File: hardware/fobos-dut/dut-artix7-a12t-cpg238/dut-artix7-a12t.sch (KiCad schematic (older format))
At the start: 4 parts

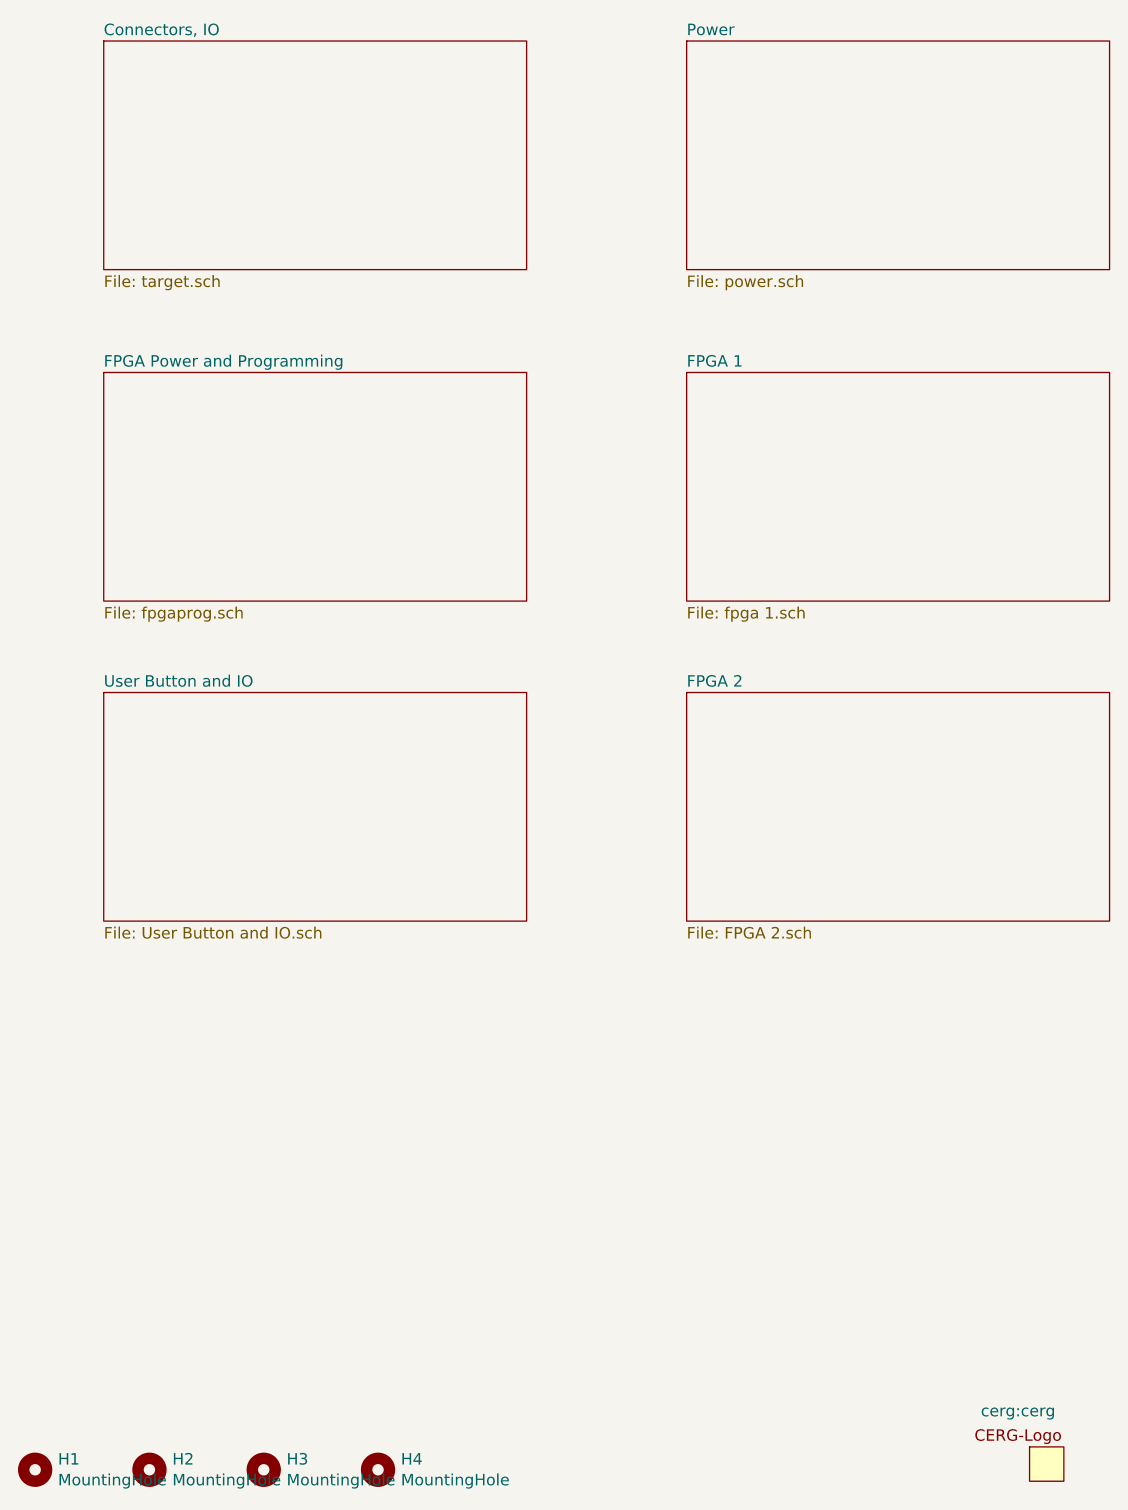
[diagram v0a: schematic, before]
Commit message: Started to rewire the CPG238 into the schematic Split FPGA Power and Programming into two sheets since new FPGA symbol explicitly displays each power pin and is much larger
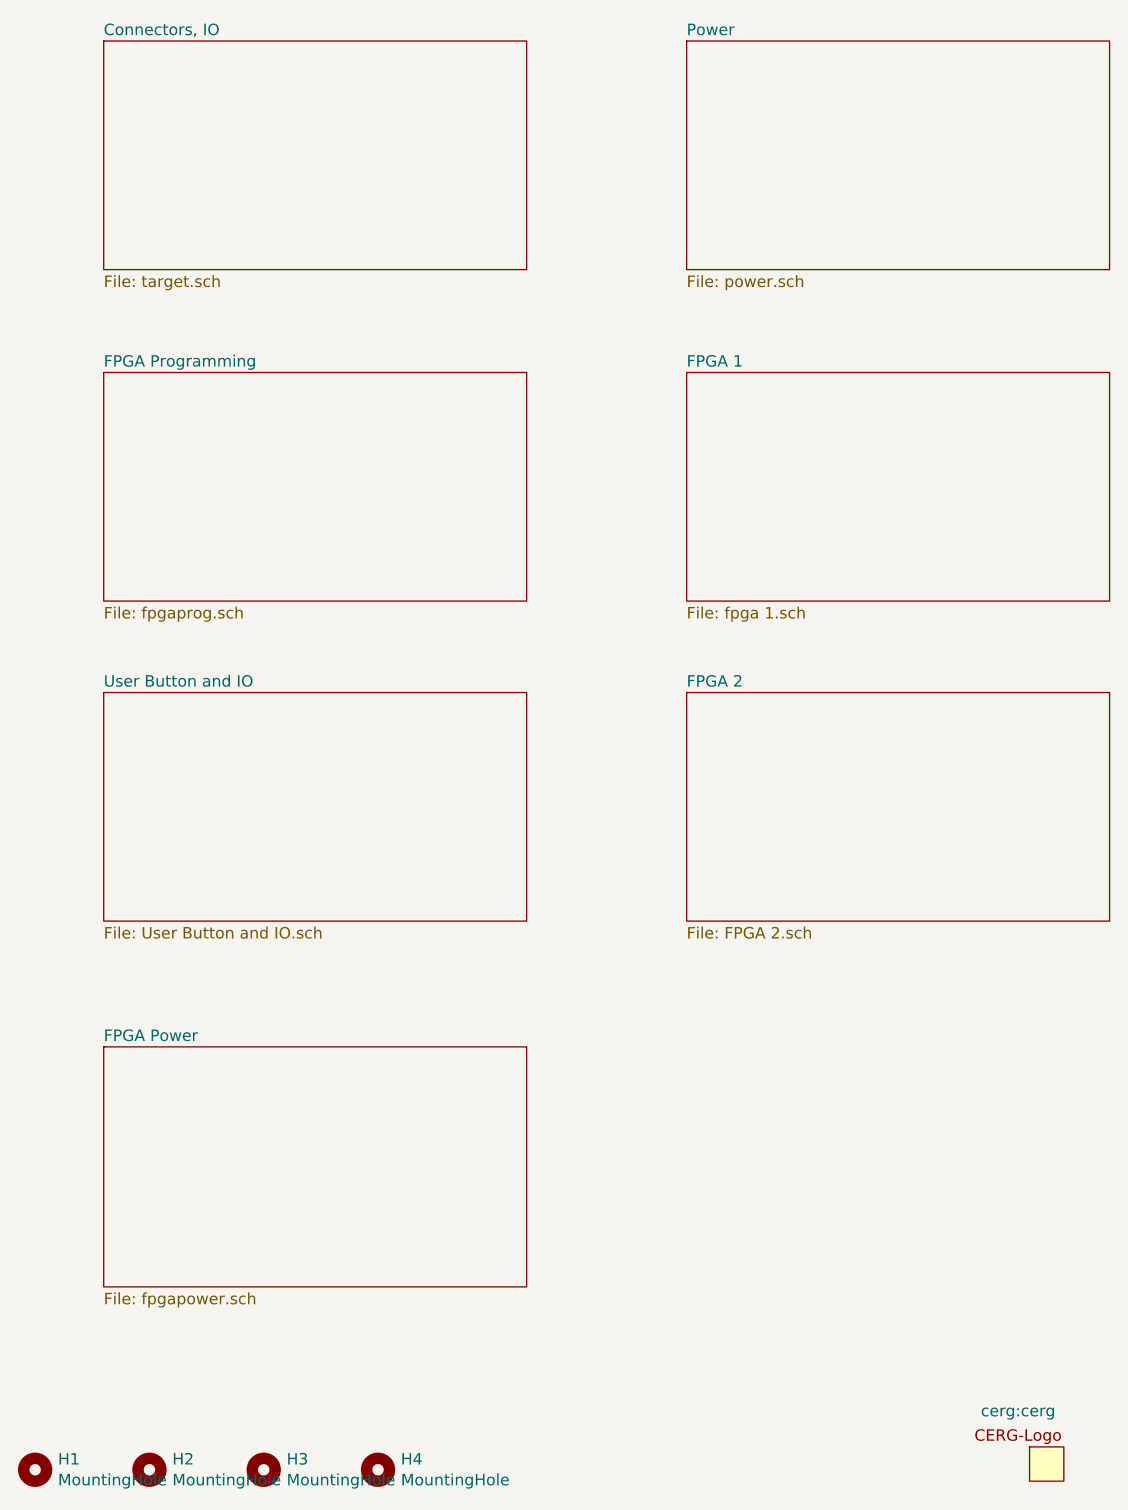
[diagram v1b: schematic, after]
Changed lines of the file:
@@
 $Descr USLetter 11000 8500
 encoding utf-8
-Sheet 1 7
+Sheet 1 8
 Title "FOBOS Artix-7 a12t DUT"
 Date "2020-07-28"
@@
 S 1550 2650 1850 1000
 U 5F3A1954
-F0 "FPGA Power and Programming" 50
+F0 "FPGA Programming" 50
 F1 "fpgaprog.sch" 50
 $EndSheet
@@
 F1 "User Button and IO.sch" 50
 $EndSheet
+$Sheet
+S 1550 5600 1850 1050
+U 60D2F94F
+F0 "FPGA Power" 50
+F1 "fpgapower.sch" 50
+$EndSheet
 $EndSCHEMATC
